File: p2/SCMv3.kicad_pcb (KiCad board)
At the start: 2 copper layers, 58.7 x 110.9 mm, 120 parts, among them IC1 40106, IC2 40106, IC3 TL082, J1 ISP, J1-OUT8 JACK-MONO-SWB, J2 Conn_01x02, J2-OUT7 JACK-MONO-SWB, J3 POWER, J3-OUT6 JACK-MONO-SWB, J4-OUT5 JACK-MONO-SWB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

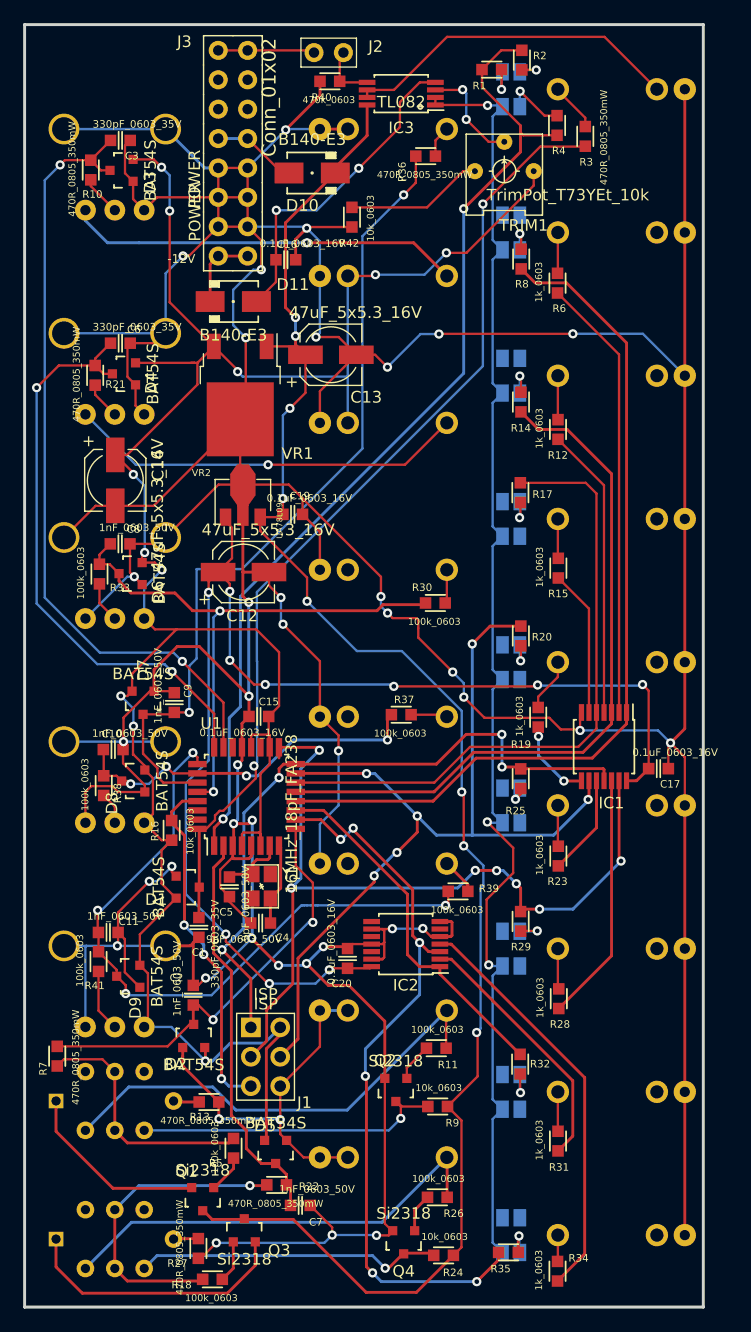
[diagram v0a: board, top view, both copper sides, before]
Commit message: replaced 9v reg with 8v reg
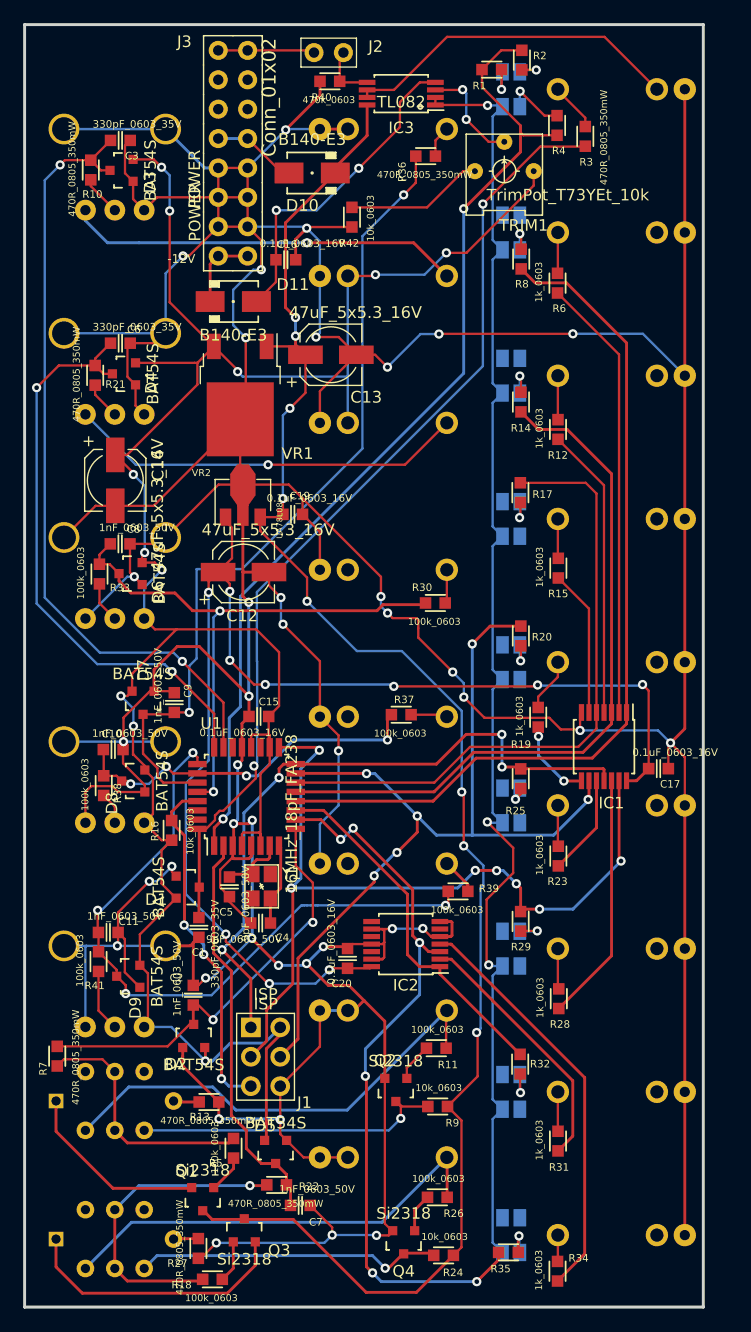
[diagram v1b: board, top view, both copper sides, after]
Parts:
- VR2: value UA78L09 -> UA78L08
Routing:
- net GND: track 669.6 -> 666.5 mm
- net Net-(D11-Pad1): track 8.67 -> 6.76 mm
- net +5V: track 209.3 -> 208.0 mm
- net /UC_OUT6_SCK: track 74.2 -> 73.3 mm
- net /UC_FAST: track 37.6 -> 37.0 mm

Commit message: nudged leds
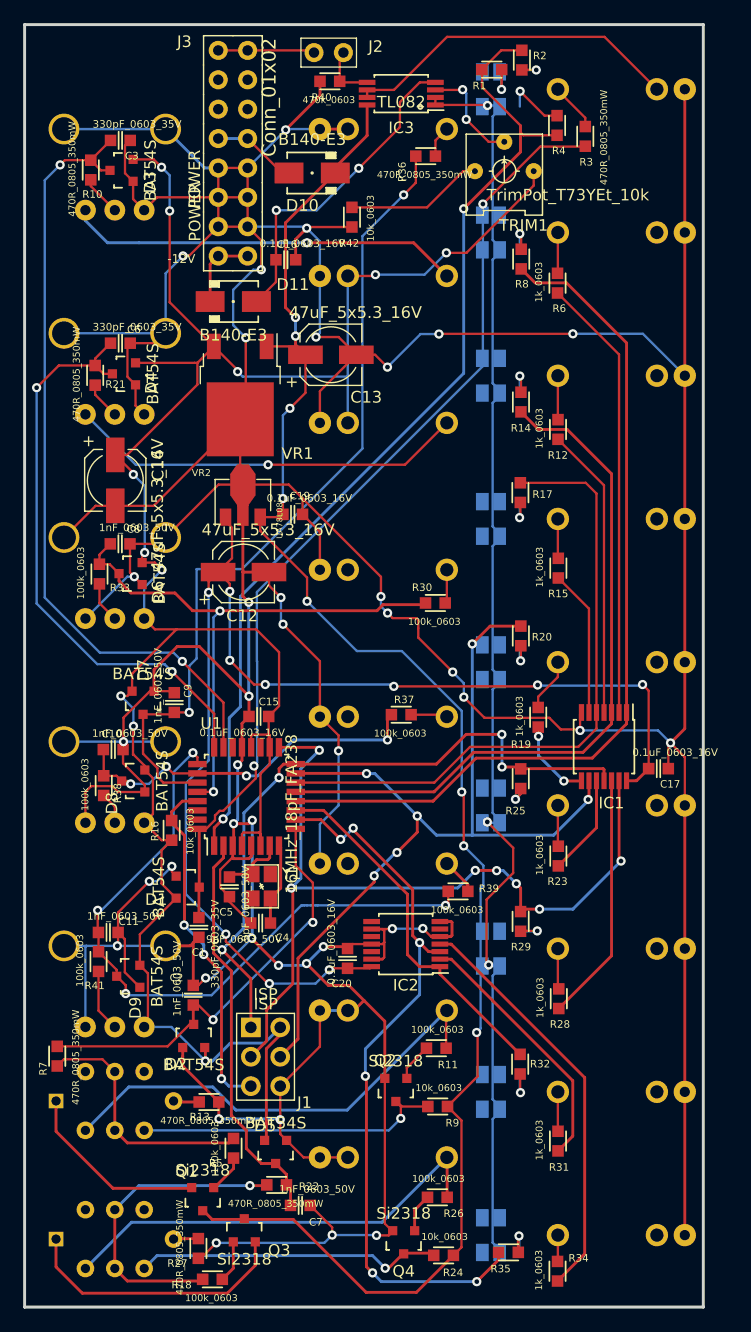
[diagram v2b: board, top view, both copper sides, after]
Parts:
- moved LED1 1.74 mm to (40.3, 104.6)
- moved LED2 1.74 mm to (40.3, 92.3)
- moved LED3 1.74 mm to (40.3, 79.9)
- moved LED4 1.74 mm to (40.3, 67.5)
- moved LED5 1.74 mm to (40.3, 55.1)
- moved LED6 1.74 mm to (40.3, 42.7)
- moved LED7 1.74 mm to (40.3, 30.4)
- moved LED8 1.74 mm to (40.3, 18.0)
- moved LED9 1.74 mm to (40.3, 5.59)
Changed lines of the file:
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@@
   )
   (footprint "4ms_LED:LED_PLCC-4" locked (layer "B.Cu")
-    (at 42.0624 92.2655 -90)
+    (at 40.31742 92.2655 -90)
     (property "ID" "")
     (property "Manufacturer" "Hebei I.T. (Shanghai)")
@@
   )
   (footprint "4ms_LED:LED_PLCC-4" locked (layer "B.Cu")
-    (at 42.0624 42.7355 -90)
+    (at 40.31742 42.7355 -90)
     (property "ID" "")
     (property "Manufacturer" "Hebei I.T. (Shanghai)")
@@
   )
   (footprint "4ms_LED:LED_PLCC-4" locked (layer "B.Cu")
-    (at 42.0624 5.588 -90)
+    (at 40.31742 5.588 -90)
     (property "ID" "")
     (property "Manufacturer" "Hebei I.T. (Shanghai)")
@@
   )
   (footprint "4ms_LED:LED_PLCC-4" locked (layer "B.Cu")
-    (at 42.0624 30.353 -90)
+    (at 40.31742 30.353 -90)
     (property "ID" "")
     (property "Manufacturer" "Hebei I.T. (Shanghai)")
@@
   )
   (footprint "4ms_LED:LED_PLCC-4" locked (layer "B.Cu")
-    (at 42.0624 67.5005 -90)
+    (at 40.31742 67.5005 -90)
     (property "ID" "")
     (property "Manufacturer" "Hebei I.T. (Shanghai)")
@@
   )
   (footprint "4ms_LED:LED_PLCC-4" locked (layer "B.Cu")
-    (at 42.0624 17.9705 -90)
+    (at 40.31742 17.9705 -90)
     (property "ID" "")
     (property "Manufacturer" "Hebei I.T. (Shanghai)")
@@
   )
   (footprint "4ms_LED:LED_PLCC-4" locked (layer "B.Cu")
-    (at 42.0624 55.118 -90)
+    (at 40.31742 55.118 -90)
     (property "ID" "")
     (property "Manufacturer" "Hebei I.T. (Shanghai)")
@@
   )
   (footprint "4ms_LED:LED_PLCC-4" locked (layer "B.Cu")
-    (at 42.0624 79.883 -90)
+    (at 40.31742 79.883 -90)
     (property "ID" "")
     (property "Manufacturer" "Hebei I.T. (Shanghai)")
@@
   )
   (footprint "4ms_LED:LED_PLCC-4" locked (layer "B.Cu")
-    (at 42.0624 104.648 -90)
+    (at 40.31742 104.648 -90)
     (property "ID" "")
     (property "Manufacturer" "Hebei I.T. (Shanghai)")

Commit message: Rerouting after nudging leds
ran DRC, no violations nor warnings
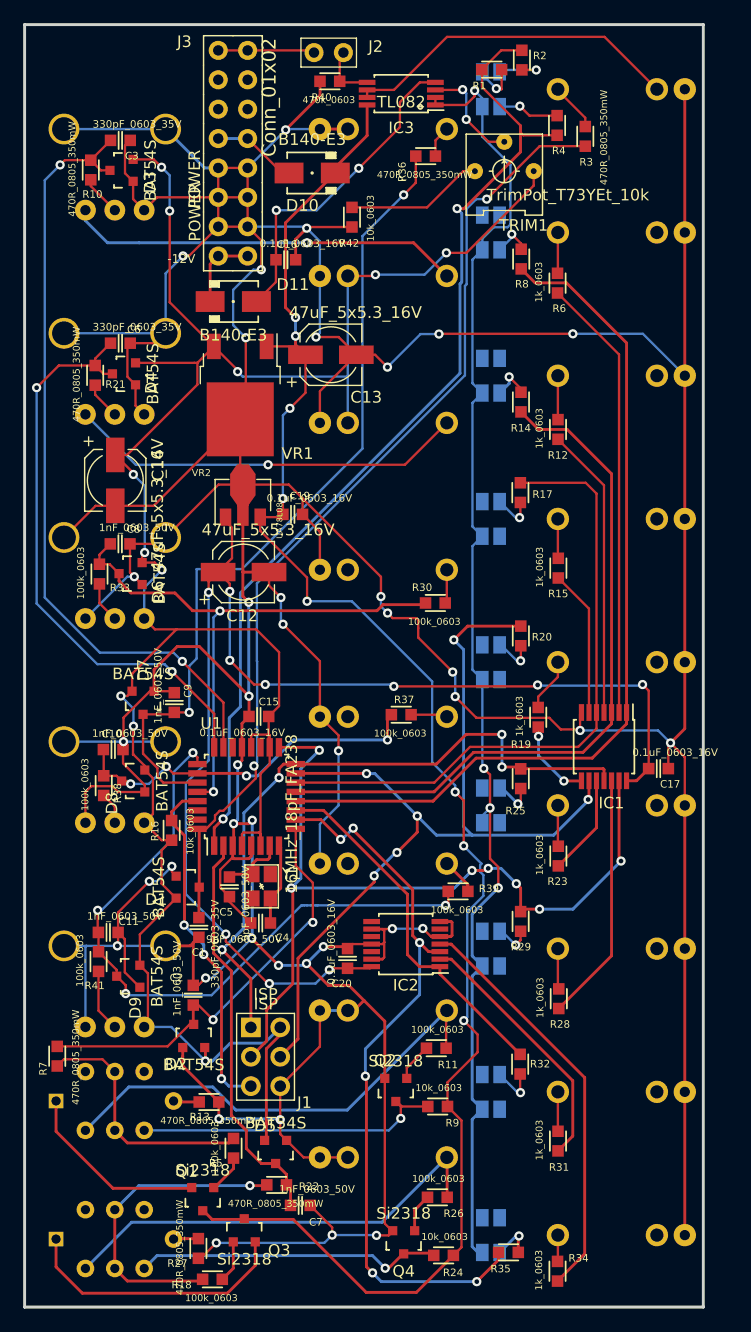
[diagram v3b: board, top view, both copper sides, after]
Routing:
- net /UC_OUT4_MOSI: track 77.6 -> 80.1 mm
- net Net-(LED9-Pad4): track 2.73 -> 4.23 mm
- net Net-(LED4-Pad4): track 2.24 -> 3.58 mm
- net +12V: track 147.7 -> 148.7 mm
- net Net-(LED5-Pad4): track 2.72 -> 3.69 mm
- net Net-(LED2-Pad4): track 3.21 -> 4.15 mm
- net Net-(LED9-Pad1): track 3.26 -> 4.13 mm
- net Net-(LED1-Pad3): track 2.90 -> 3.71 mm
- net /UC_LED_IN: track 86.8 -> 87.5 mm
- net Net-(LED8-Pad3): track 2.78 -> 3.42 mm
- net /UC_CLK_IN: track 83.5 -> 84.0 mm
- net Net-(LED7-Pad3): track 2.92 -> 3.48 mm
- net Net-(LED6-Pad4): track 2.73 -> 3.30 mm
- net /VREF: track 115.0 -> 115.5 mm, vias 3 -> 4

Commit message: p2: Added text to Fsilk and exported gerbers
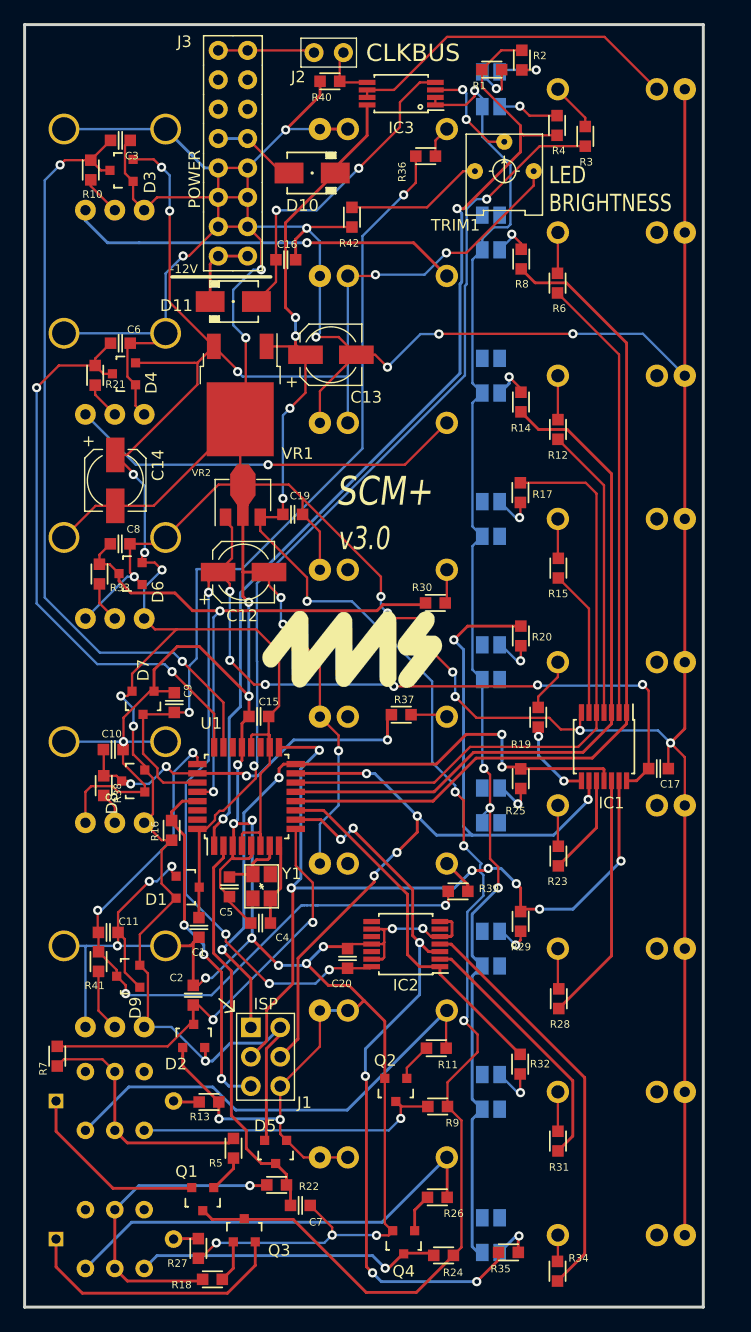
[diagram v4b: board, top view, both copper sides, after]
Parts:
- added G***: LOGO, 4ms_Symbol:4msLogo_15.5x6.6mm, F.Cu at (28.3, 54.0)
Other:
- board text added: "CLKBUS"
- board text added: "LED BRIGHTNESS"
- board text added: "SCM+"
- board text added: "v3.0"

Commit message: SCMBOV3 updates
Updated resistor value to fix blueness of white led 
Changed the pot footprints on schematic and pcb 
Flipped shuffle/skip/pw pots so they are not longer backward on sch and pcb
sorry if I staged too many things I was not sure...
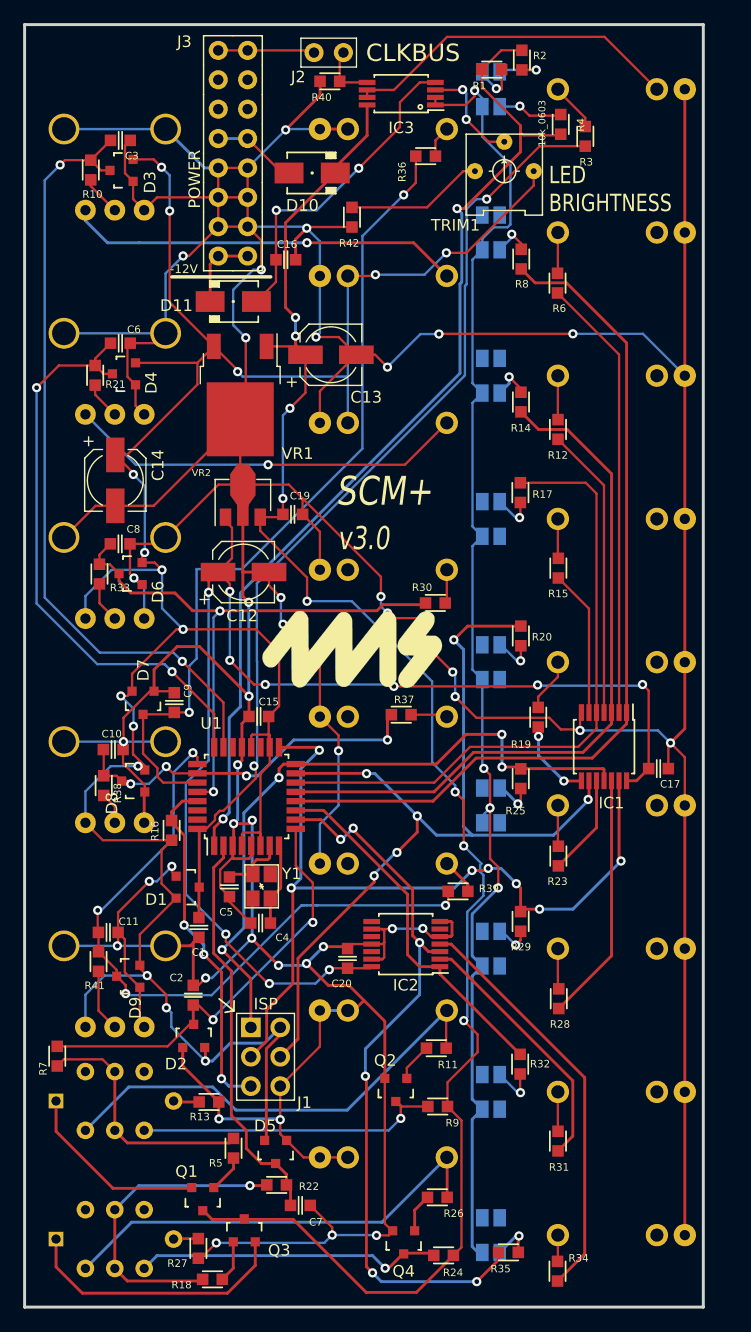
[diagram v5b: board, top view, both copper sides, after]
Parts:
- PPW1, PROTATE1, PSHUFFLE1, PSKIP1, PSLIP1: value 9mm_CtrDet_10k_DShaft -> 9mm_NoDet_100k_Knurled_Lined; footprint 4ms_Potentiometer:Pot_9mm_Dshaft_Det -> 4ms_Potentiometer:Pot_9mm_Knurl_NoDet
- R4: value 4.7k_0603 -> 10k_0603
- moved R4 0.33 mm to (46.3, 8.63)
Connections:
- PPW1 pad 1: +5V -> GND
- PPW1 pad 3: GND -> +5V
- PSHUFFLE1 pad 1: +5V -> GND
- PSHUFFLE1 pad 3: GND -> +5V
- PSKIP1 pad 1: +5V -> GND
- PSKIP1 pad 3: GND -> +5V
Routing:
- net +5V: track 208.0 -> 231.4 mm, vias 11 -> 15
- net GND: track 666.9 -> 656.1 mm
